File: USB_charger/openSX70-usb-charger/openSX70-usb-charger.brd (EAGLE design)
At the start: 160 x 100 mm, 11 parts, among them IC1 LD117AS50TR

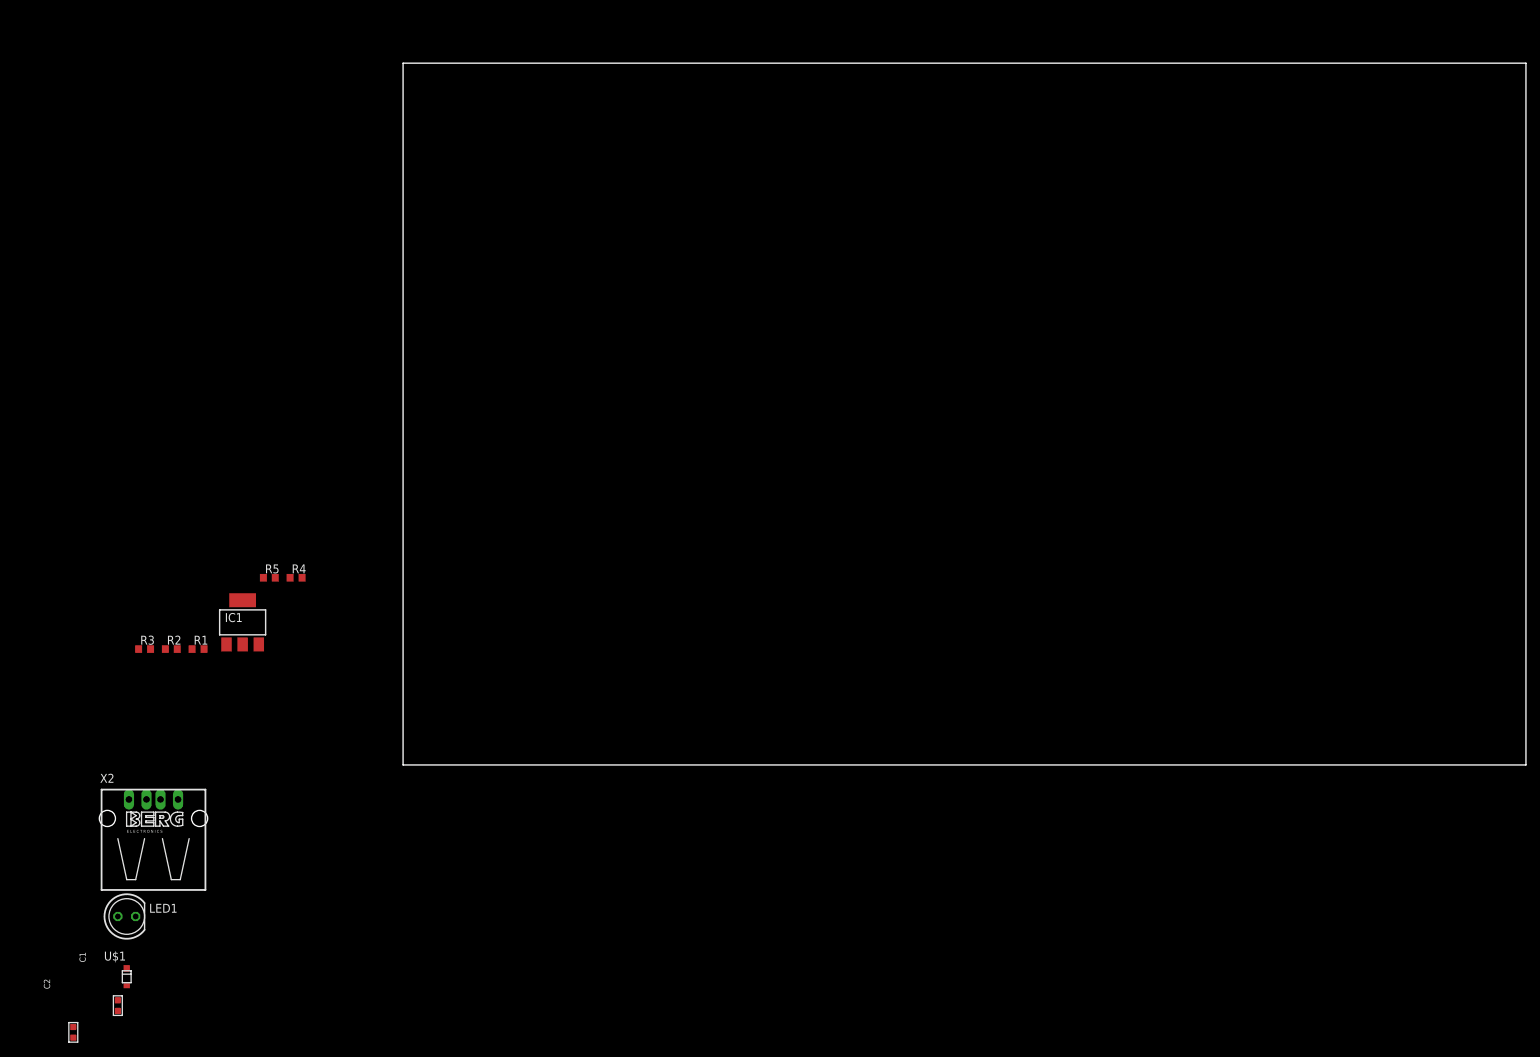
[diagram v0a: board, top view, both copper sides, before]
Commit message: added photo-sized pcb outline to charger
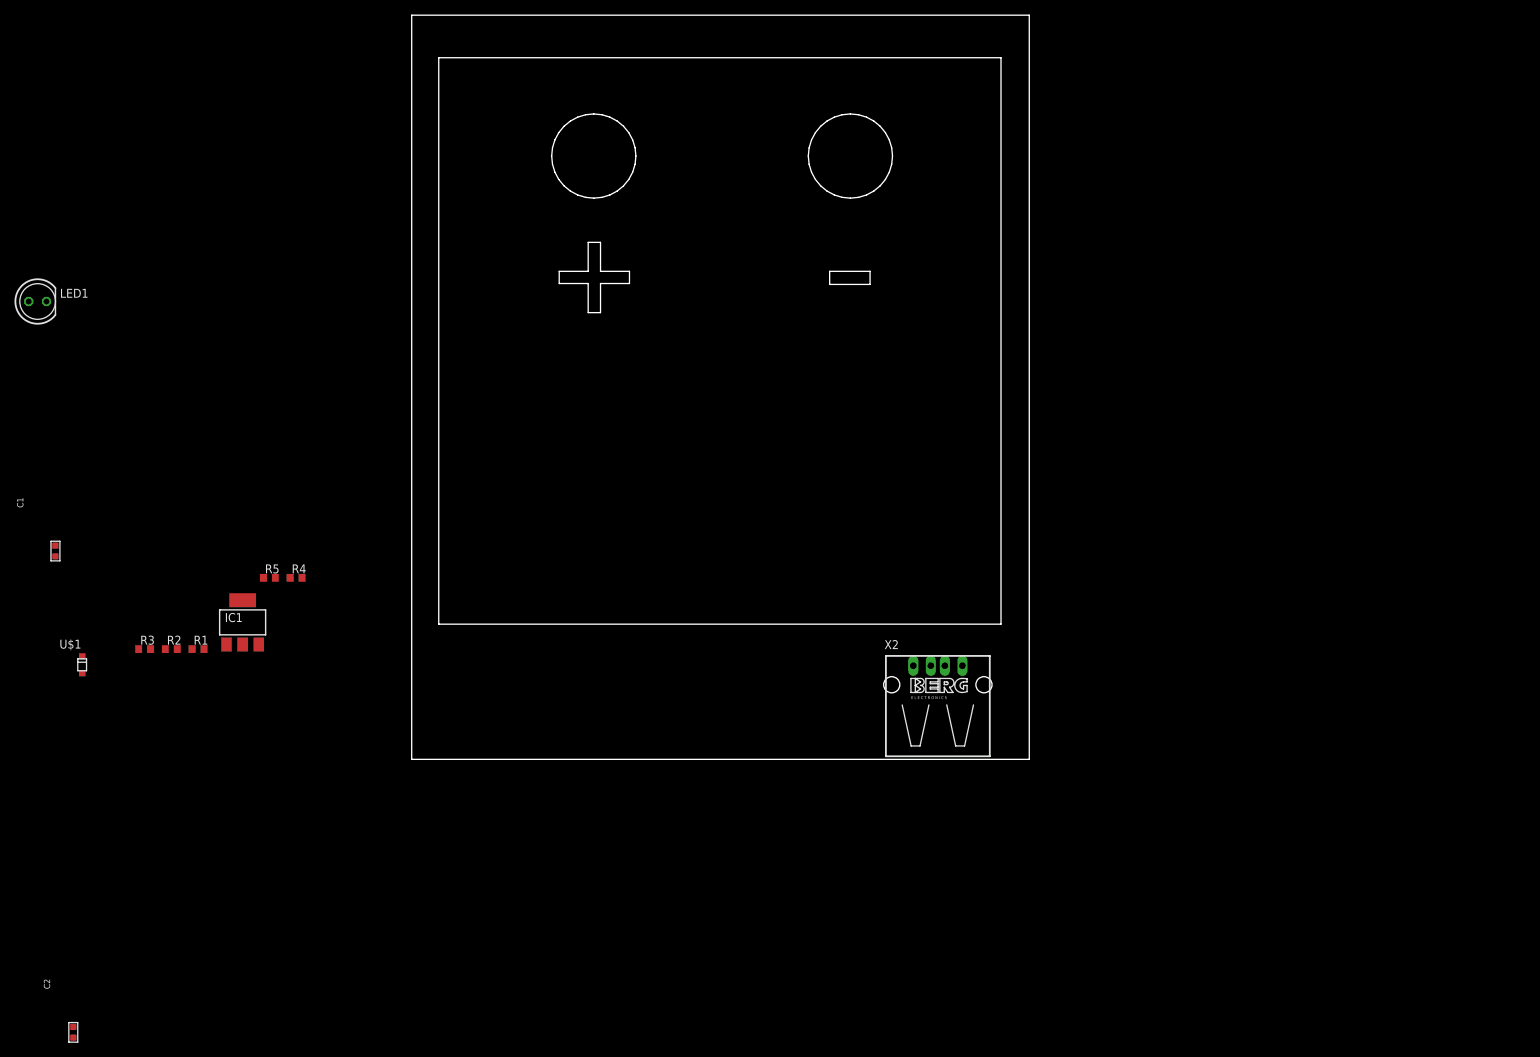
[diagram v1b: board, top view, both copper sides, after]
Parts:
- moved X2 113.4 mm to (76.2, 11.4)
- moved LED1 88.5 mm to (-52.1, 66.0)
- moved C1 65.4 mm to (-49.5, 30.5)
- moved U$1 44.9 mm to (-45.7, 14.0)
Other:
- board size 160 x 100 mm -> 88 x 106 mm

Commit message: Working on the bench
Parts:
- moved LED1 126.1 mm to (59.7, 7.62)
- moved R1 72.2 mm to (41.9, 3.81)
- moved C2 71.9 mm to (6.35, 10.2), turned to 180 degrees
- moved R3 68.5 mm to (30.5, 3.81), turned to 180 degrees
- moved R2 64.1 mm to (30.5, 7.62)
- moved C1 61.4 mm to (6.35, 5.08), turned to 180 degrees
- moved R5 60.4 mm to (36.8, 3.81), turned to 180 degrees
- moved R4 55.4 mm to (36.8, 7.62)
- moved U$1 49.9 mm to (3.81, 7.62)
- moved IC1 39.4 mm to (14.0, 6.35), turned to 270 degrees

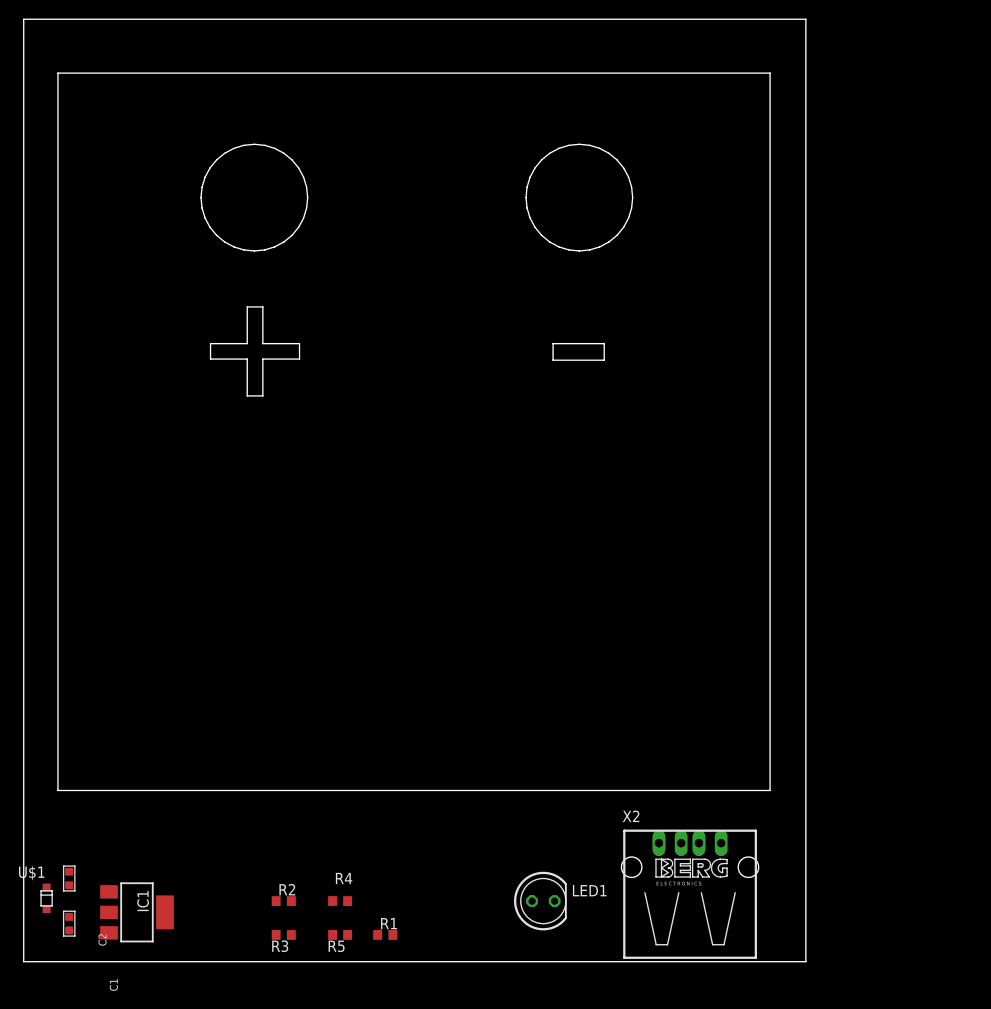
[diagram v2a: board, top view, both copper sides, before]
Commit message: new USB charger design
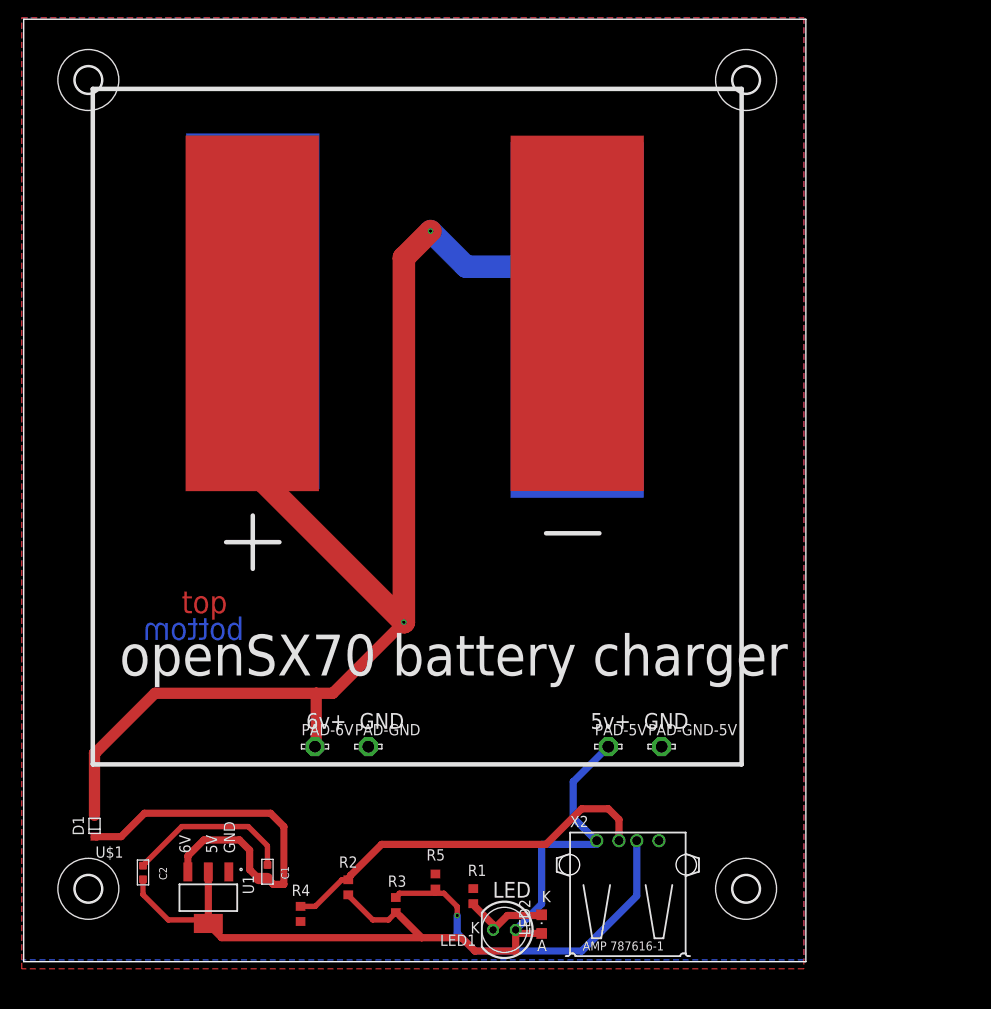
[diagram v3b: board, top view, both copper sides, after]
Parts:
- removed IC1: LD117AS50TR, v-reg:SOT223
- added H1, H2, H3, H4: MOUNT-HOLE3.0, holes:3,0
- added LED2: (no value), led:CHIPLED_0805
- added PAD-5V, PAD-6V, PAD-GND, PAD-GND-5V: LSP13, solpad:LSP13
- added U$2, U$3, U$4, U$5: BATTERY-PAD, _openSX70:BATTERY-PAD
- added U1: LD1117S50TR, Common-Parts-Library-Eagle:LD1117S50TR_SOT230P700X180-4N
- X2: device con-berg:PN87520 -> con-amp:USB
- moved C1 23.1 mm to (28.6, 10.9), turned to 0 degrees
- moved R3 13.1 mm to (43.1, 7.17), turned to 270 degrees
- moved R5 12.3 mm to (47.5, 9.82), turned to 270 degrees
- moved X2 12.2 mm to (69.2, 1.43)
- moved R1 10.8 mm to (51.8, 8.18), turned to 270 degrees
- moved U$1 10.3 mm to (9.19, 16.4), turned to 180 degrees
- moved C2 8.33 mm to (14.7, 10.8), turned to 0 degrees
- moved R2 7.42 mm to (37.7, 9.18), turned to 270 degrees
- moved LED1 5.45 mm to (55.3, 4.38), turned to 180 degrees
- moved R4 4.68 mm to (32.4, 6.17), turned to 90 degrees
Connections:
- new net N$4: C1.1, C2.1
- net 6V-BAT: now also PAD-6V.MP, U$2.P$2, U$4.P$2
- net 6VIN: now also U1.3; no longer IC1.4
- net GND: now also PAD-GND-5V.MP, PAD-GND.MP, U$3.P$2, U$5.P$2, U1.1; no longer C1.1, C2.1, IC1.1
- net N$1: now also LED2.C
- net N$2: now also LED2.A, PAD-5V.MP, U1.2, U1.4; no longer IC1.3
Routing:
- net 6V-BAT: track 0.00 -> 165.2 mm, vias 0 -> 2
- net N$2: track 0.00 -> 99.3 mm
- net 6VIN: track 0.00 -> 46.2 mm
- net N$3: track 0.00 -> 43.3 mm
- net N$5: track 0.00 -> 41.0 mm, vias 0 -> 1
- net N$4: track 0.00 -> 18.9 mm
- net N$1: track 0.00 -> 10.1 mm
- added copper zone on layer 1, net GND
- added copper zone on layer 16, net GND
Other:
- outline, holes or cut-outs redrawn
- board text added: "5V"
- board text added: "5v+"
- board text added: "6V"
- board text added: "6v+"
- board text added: "A"
- board text added: "D1"
- board text added: "GND"
- board text added: "K"
- board text added: "LED"
- board text added: "bottom"
- board text added: "openSX70 battery charger"
- board text added: "top"

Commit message: minor changes, waiting for PJK on new regulator
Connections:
- removed net N$4: C1.1, C2.1
- net GND: now also C1.1, C2.1
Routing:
- net N$4: track 18.9 -> 0.00 mm
- net GND: track 0.32 -> 19.2 mm
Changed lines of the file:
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@@
 <element name="C2" library="Seeed-Capacitor" library_urn="urn:adsk.eagle:library:464" package="C0603" package3d_urn="urn:adsk.eagle:package:32378/1" value="100nf" x="14.65" y="10.84">
 <attribute name="MPN" value="CC0603KRX7R9BB104" x="9.57" y="17.19" size="1.778" layer="27" display="off"/>
+<attribute name="NAME" x="16.459" y="11.46" size="0.889" layer="25" font="vector" ratio="11" rot="R270"/>
 <attribute name="NAME" x="9.316" y="18.46" size="0.635" layer="33" ratio="10" rot="R270"/>
-<attribute name="NAME" x="16.459" y="11.46" size="0.889" layer="25" font="vector" ratio="11" rot="R270"/>
 <attribute name="VALUE" x="7.9825" y="18.46" size="0.635" layer="27" ratio="10" rot="R270"/>
 </element>
@@
 <vertex x="1" y="107"/>
 </polygon>
+<contactref element="C1" pad="1"/>
+<contactref element="C2" pad="1"/>
+<wire x1="19" y1="16" x2="15" y2="12" width="0.6096" layer="1"/>
+<wire x1="26.5" y1="16" x2="19" y2="16" width="0.6096" layer="1"/>
+<wire x1="28.60714375" y1="13.89285625" x2="26.5" y2="16" width="0.6096" layer="1"/>
+<wire x1="15" y1="12" x2="14.65" y2="11.602" width="0.6096" layer="1"/>
+<wire x1="28.65" y1="13.802" x2="28.65" y2="11.682" width="0.6096" layer="1"/>
+<wire x1="28.65" y1="13.802" x2="28.60714375" y2="13.89285625" width="0.1524" layer="1"/>
 </signal>
 <signal name="6VIN">
@@
 <wire x1="63.5508" y1="77.8764" x2="63.5" y2="79" width="0.1524" layer="16"/>
 </signal>
-<signal name="N$4">
-<contactref element="C1" pad="1"/>
-<contactref element="C2" pad="1"/>
-<wire x1="19" y1="16" x2="15" y2="12" width="0.6096" layer="1"/>
-<wire x1="26.5" y1="16" x2="19" y2="16" width="0.6096" layer="1"/>
-<wire x1="28.60714375" y1="13.89285625" x2="26.5" y2="16" width="0.6096" layer="1"/>
-<wire x1="15" y1="12" x2="14.65" y2="11.602" width="0.6096" layer="1"/>
-<wire x1="28.65" y1="13.802" x2="28.65" y2="11.682" width="0.6096" layer="1"/>
-<wire x1="28.65" y1="13.802" x2="28.60714375" y2="13.89285625" width="0.1524" layer="1"/>
-</signal>
 </signals>
